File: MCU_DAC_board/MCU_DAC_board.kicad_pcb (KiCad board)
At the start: 2 copper layers, 100 x 100 mm, 95 parts, among them J1 Conn_02x04_Odd_Even, J11 105-0752-001, J12 Conn_01x03_Pin, J2 Conn_02x04_Odd_Even, J3 Conn_02x04_Odd_Even, J4 Conn_02x04_Odd_Even, J5 54-00127, J6 105-0752-001, J7 Screw_Terminal_01x02, J8 Screw_Terminal_01x02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

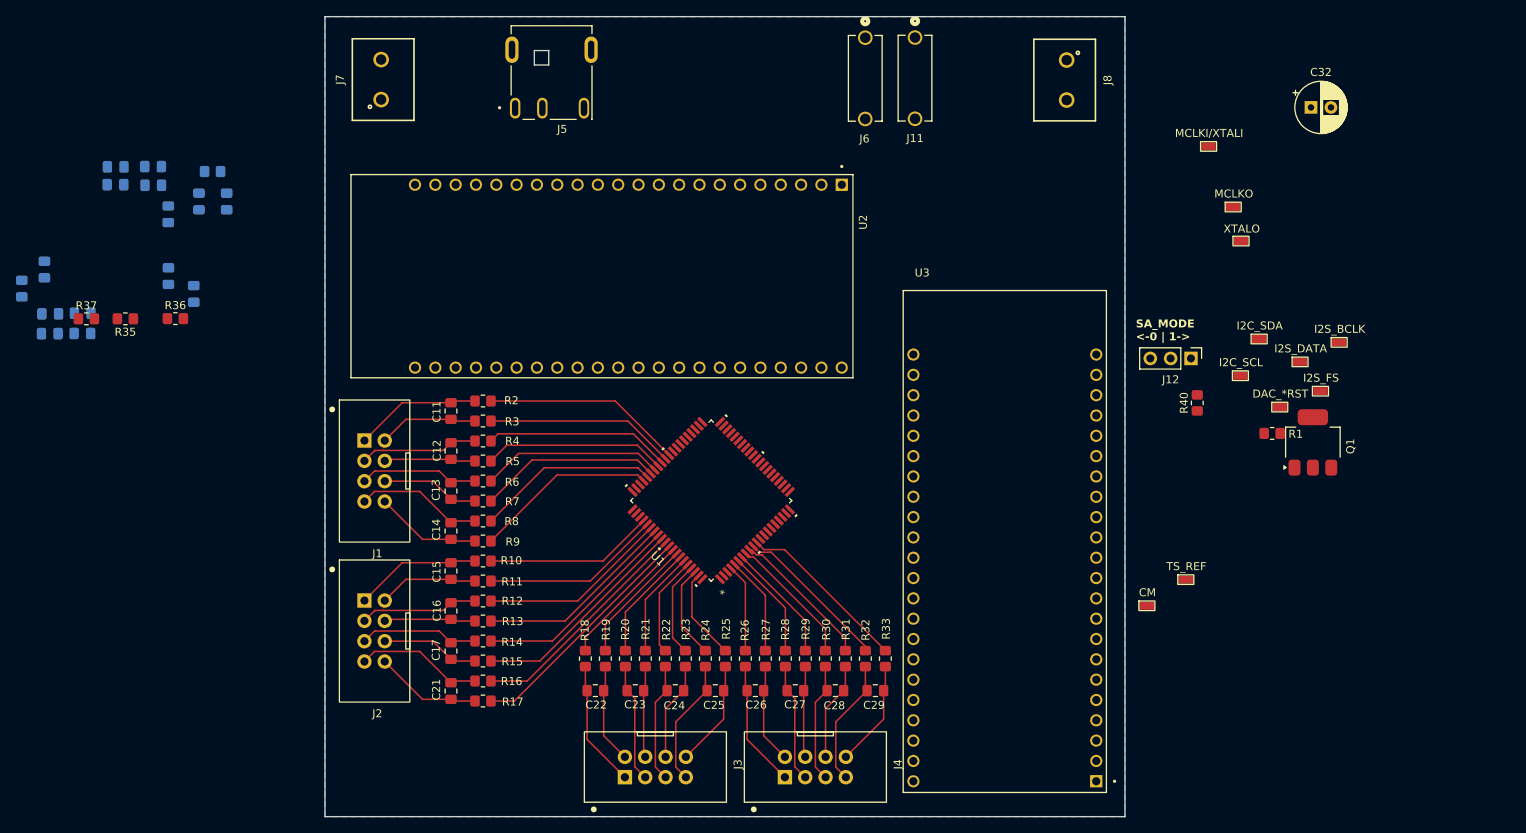
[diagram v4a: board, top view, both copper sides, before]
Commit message: Changed to 4 layer board
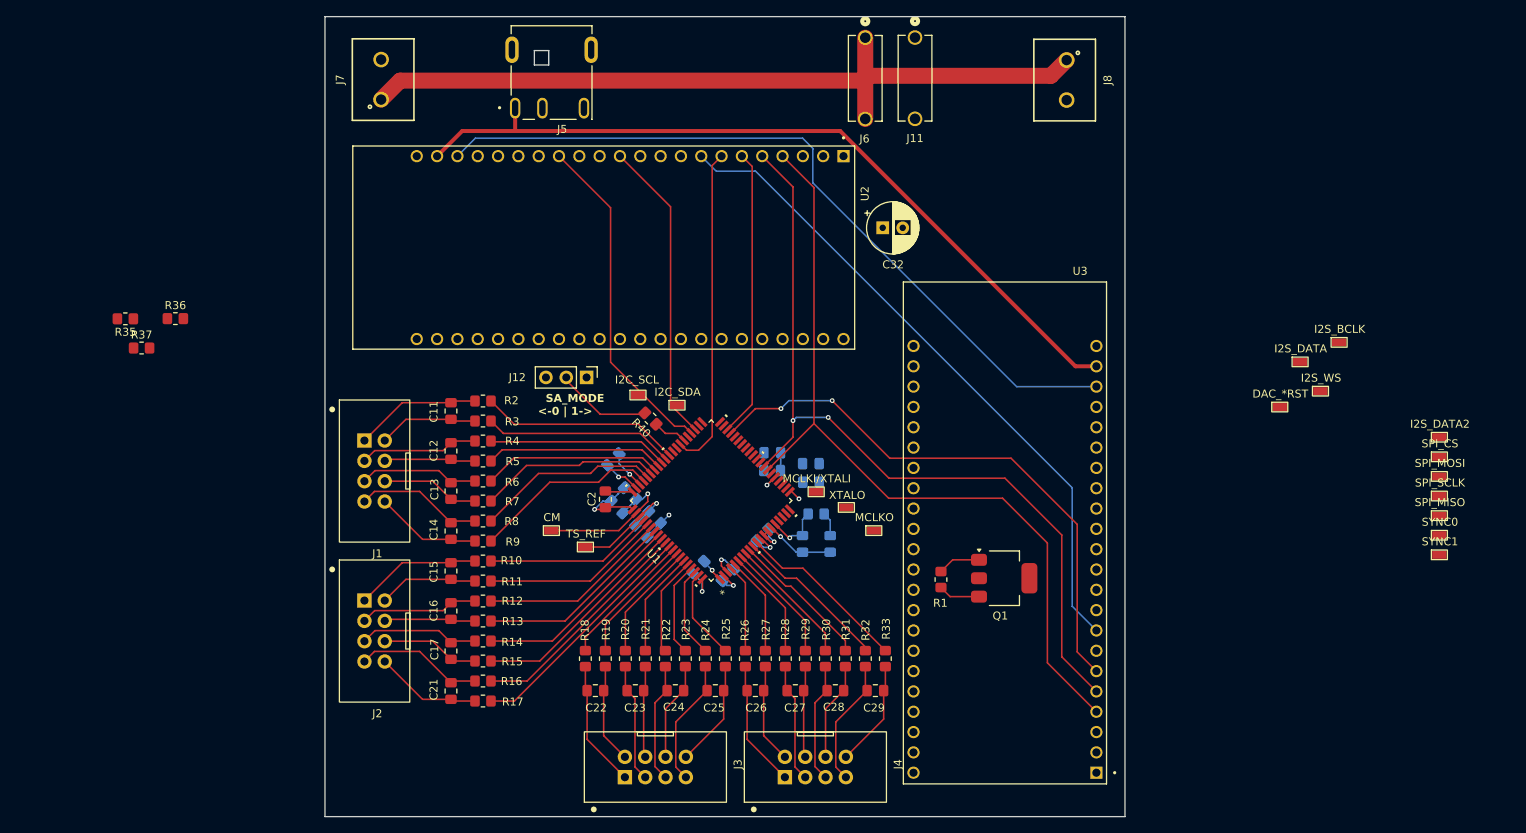
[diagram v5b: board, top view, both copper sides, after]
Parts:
- added TP12: I2S_DATA2, project_lib:TP_1.8x1mm, F.Cu at (232.4, 111.4)
- added TP13: SPI_CS, project_lib:TP_1.8x1mm, F.Cu at (232.4, 113.9)
- added TP14: SPI_MOSI, project_lib:TP_1.8x1mm, F.Cu at (232.4, 116.3)
- added TP15: SPI_SCLK, project_lib:TP_1.8x1mm, F.Cu at (232.4, 118.8)
- added TP16: SPI_MISO, project_lib:TP_1.8x1mm, F.Cu at (232.4, 121.2)
- added TP17: SYNC0, project_lib:TP_1.8x1mm, F.Cu at (232.4, 123.7)
- added TP18: SYNC1, project_lib:TP_1.8x1mm, F.Cu at (232.4, 126.1)
- C2: moved to F.Cu
- TP5: value I2S_FS -> I2S_WS
- moved C18 90.2 mm to (153.8, 114.7)
- moved C20 90.2 mm to (153.8, 117.1)
- moved C10 89.5 mm to (149.0, 115.6)
- moved C19 89.5 mm to (149.0, 113.4)
- moved C31 86.7 mm to (152.8, 124.8)
- moved C30 86.7 mm to (156.2, 124.8)
- moved R34 86.7 mm to (154.5, 121.0)
- moved C1 84.5 mm to (147.8, 123.7), turned to 45 degrees
- moved C8 79.3 mm to (143.4, 128.6), turned to 45 degrees
- moved C2 77.6 mm to (128.1, 119.2)
- moved J12 75.6 mm to (125.8, 104.0)
- moved TP9 75.3 mm to (132.2, 106.2)
- moved C5 75.3 mm to (131.2, 118.5), turned to 135 degrees
- moved TP10 75.2 mm to (125.6, 125.2)
- moved C6 75.1 mm to (134.3, 121.5), turned to -45 degrees
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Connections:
- net /GPIO6 renamed /I2S_DATA1
- Q1 pad 1: +2V5 -> /VDRIVE
- Q1 pad 2: /VDRIVE -> +2V5
- R35 pad 2: /GPIO8 -> /I2C_SDA
- R37 pad 2: /GPIO9 -> /I2C_SCL
- TP4 pad 1: /GPIO4 -> /I2S_BCLK
- TP5 pad 1: /GPIO5 -> /I2S_WS
- TP8 pad 1: /GPIO8 -> /I2C_SDA
- TP9 pad 1: /GPIO9 -> /I2C_SCL
- U1 pad 27: /GPIO4 -> /I2S_BCLK
- U1 pad 28: /GPIO5 -> /I2S_WS
- U1 pad 37: unconnected-(U1-DSDATA2-Pad37) -> /I2S_DATA2
- U1 pad 43: /GPIO8 -> /I2C_SDA
- U1 pad 44: /GPIO9 -> /I2C_SCL
- U2 pad J1_10: /GPIO17 -> unconnected-(U2-GPIO17-PadJ1_10)
- U2 pad J1_11: /GPIO18 -> unconnected-(U2-GPIO18-PadJ1_11)
- U2 pad J1_12: /GPIO8 -> /I2C_SDA
- U2 pad J1_13: /GPIO3 -> unconnected-(U2-GPIO3-PadJ1_13)
- U2 pad J1_14: /GPIO46 -> unconnected-(U2-GPIO46-PadJ1_14)
- U2 pad J1_15: /GPIO9 -> /I2C_SCL
- U2 pad J1_16: /GPIO10 -> /SPI_CS
- U2 pad J1_17: /GPIO11 -> /SPI_MOSI
- U2 pad J1_18: /GPIO12 -> /SPI_SCLK
- U2 pad J1_19: /GPIO13 -> /SPI_MISO
- U2 pad J1_20: /GPIO14 -> /SYNC0
- U2 pad J1_4: /GPIO4 -> /I2S_BCLK
- U2 pad J1_5: /GPIO5 -> /I2S_WS
- U2 pad J1_8: /GPIO15 -> /SYNC1
- U2 pad J1_9: /GPIO16 -> unconnected-(U2-GPIO16-PadJ1_9)
- U2 pad J3_10: /GPIO38 -> unconnected-(U2-GPIO38-PadJ3_10)
- U2 pad J3_11: /GPIO37 -> unconnected-(U2-GPIO37-PadJ3_11)
- U2 pad J3_12: /GPIO36 -> unconnected-(U2-GPIO36-PadJ3_12)
- U2 pad J3_13: /GPIO35 -> unconnected-(U2-GPIO35-PadJ3_13)
- U2 pad J3_14: /GPIO0 -> unconnected-(U2-GPIO0-PadJ3_14)
- U2 pad J3_15: /GPIO45 -> unconnected-(U2-GPIO45-PadJ3_15)
- U2 pad J3_16: /GPIO48 -> unconnected-(U2-GPIO48-PadJ3_16)
- U2 pad J3_17: /GPIO47 -> unconnected-(U2-GPIO47-PadJ3_17)
- U2 pad J3_18: /GPIO21 -> unconnected-(U2-GPIO21-PadJ3_18)
- U2 pad J3_19: /GPIO20 -> unconnected-(U2-USB_D+/GPIO20-PadJ3_19)
- U2 pad J3_2: /GPIO43 -> unconnected-(U2-U0TXD/GPIO43-PadJ3_2)
- U2 pad J3_20: /GPIO19 -> unconnected-(U2-USB_D-/GPIO19-PadJ3_20)
- U2 pad J3_3: /GPIO44 -> unconnected-(U2-U0RXD/GPIO44-PadJ3_3)
- U2 pad J3_4: /GPIO1 -> unconnected-(U2-GPIO1-PadJ3_4)
- U2 pad J3_5: /GPIO2 -> unconnected-(U2-GPIO2-PadJ3_5)
- U2 pad J3_6: /GPIO42 -> unconnected-(U2-MTMS/GPIO42-PadJ3_6)
- U2 pad J3_7: /GPIO41 -> unconnected-(U2-MTDI/GPIO41-PadJ3_7)
- U2 pad J3_8: /GPIO40 -> unconnected-(U2-MTDO/GPIO40-PadJ3_8)
- U2 pad J3_9: /GPIO39 -> unconnected-(U2-MTCK/GPIO39-PadJ3_9)
- U3 pad J1_12: unconnected-(U3-GPIO8-PadJ1_12) -> /I2C_SDA
- U3 pad J1_15: unconnected-(U3-GPIO9-PadJ1_15) -> /I2C_SCL
- U3 pad J1_16: unconnected-(U3-GPIO10-PadJ1_16) -> /SPI_CS
- U3 pad J1_17: unconnected-(U3-GPIO11-PadJ1_17) -> /SPI_MOSI
- U3 pad J1_18: unconnected-(U3-GPIO12-PadJ1_18) -> /SPI_SCLK
- U3 pad J1_19: unconnected-(U3-GPIO13-PadJ1_19) -> /SPI_MISO
- U3 pad J1_20: unconnected-(U3-GPIO14-PadJ1_20) -> /SYNC0
- U3 pad J1_21: unconnected-(U3-5V0-PadJ1_21) -> +5V
- U3 pad J1_22: unconnected-(U3-GND-PadJ1_22) -> GND
- U3 pad J1_4: unconnected-(U3-GPIO4-PadJ1_4) -> /I2S_BCLK
- U3 pad J1_5: unconnected-(U3-GPIO5-PadJ1_5) -> /I2S_WS
- U3 pad J1_6: unconnected-(U3-GPIO6-PadJ1_6) -> /I2S_DATA2
- U3 pad J1_7: unconnected-(U3-GPIO7-PadJ1_7) -> /DAC_*RST
- U3 pad J1_8: unconnected-(U3-GPIO15-PadJ1_8) -> /SYNC1
- U3 pad J3_1: unconnected-(U3-GND__1-PadJ3_1) -> GND
- U3 pad J3_21: unconnected-(U3-GND__2-PadJ3_21) -> GND
- U3 pad J3_22: unconnected-(U3-GND__3-PadJ3_22) -> GND
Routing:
- net /I2S_WS: track 0.00 -> 103.0 mm, vias 0 -> 2
- net /I2S_BCLK: track 0.00 -> 102.2 mm
- net +5V: track 0.00 -> 98.8 mm
- net +24V: track 0.00 -> 97.9 mm
- net /SYNC0: track 0.00 -> 96.2 mm
- net /SYNC1: track 0.00 -> 82.6 mm
- net /I2S_DATA2: track 0.00 -> 70.7 mm, vias 0 -> 2
- net /I2C_SCL: track 0.00 -> 42.2 mm
- net /DAC_*RST: track 0.00 -> 40.5 mm
- net /I2C_SDA: track 0.00 -> 38.0 mm
- net /I2S_DATA1: track 0.00 -> 36.0 mm
- net +3V3: track 0.00 -> 23.8 mm, vias 0 -> 4
- net GND: track 0.00 -> 23.5 mm, vias 0 -> 5
- net Net-(U1-CM): track 0.00 -> 18.6 mm, vias 0 -> 1
- net Net-(U1-TS_REF): track 0.00 -> 15.0 mm, vias 0 -> 1
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- added copper zone on In2.Cu, net +3V3
- added copper zone on In1.Cu, net GND
- removed copper zone on B.Cu, net GND
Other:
- copper layers 2 -> 4

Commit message: Amp board final draft
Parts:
- moved R35 80.5 mm to (148.6, 93.1), turned to 90 degrees
- moved R36 78.2 mm to (152.5, 94.9), turned to -90 degrees
- moved R37 74.2 mm to (143.8, 91.5)
- moved J7 32.2 mm to (132.3, 66.5), turned to -90 degrees
- moved J5 20.7 mm to (100.7, 63.7)
- moved Q1 11.7 mm to (178.3, 117.4)
- moved R1 11.7 mm to (170.4, 117.6)
- moved TP12 11.5 mm to (236.6, 100.7)
- moved TP13 11.5 mm to (236.6, 103.2)
- moved TP17 11.5 mm to (236.6, 113.0)
- moved TP18 11.5 mm to (236.6, 115.4)
- moved TP4 11.5 mm to (224.0, 88.8)
- moved TP6 11.5 mm to (216.6, 96.9)
- moved TP14 11.5 mm to (236.6, 105.6)
- moved TP15 11.5 mm to (236.6, 108.1)
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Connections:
- U2 pad J1_12: /I2C_SDA -> unconnected-(U2-GPIO8-PadJ1_12)
- U2 pad J1_15: /I2C_SCL -> unconnected-(U2-GPIO9-PadJ1_15)
- U2 pad J1_16: /SPI_CS -> unconnected-(U2-GPIO10-PadJ1_16)
- U2 pad J1_17: /SPI_MOSI -> unconnected-(U2-GPIO11-PadJ1_17)
- U2 pad J1_18: /SPI_SCLK -> unconnected-(U2-GPIO12-PadJ1_18)
- U2 pad J1_19: /SPI_MISO -> unconnected-(U2-GPIO13-PadJ1_19)
- U2 pad J1_20: /SYNC0 -> unconnected-(U2-GPIO14-PadJ1_20)
- U2 pad J1_4: /I2S_BCLK -> unconnected-(U2-GPIO4-PadJ1_4)
- U2 pad J1_5: /I2S_WS -> unconnected-(U2-GPIO5-PadJ1_5)
- U2 pad J1_6: /I2S_DATA1 -> unconnected-(U2-GPIO6-PadJ1_6)
- U2 pad J1_7: /DAC_*RST -> unconnected-(U2-GPIO7-PadJ1_7)
- U2 pad J1_8: /SYNC1 -> unconnected-(U2-GPIO15-PadJ1_8)
- U2 pad J3_2: unconnected-(U2-U0TXD/GPIO43-PadJ3_2) -> /USART_TX
- U2 pad J3_3: unconnected-(U2-U0RXD/GPIO44-PadJ3_3) -> /USART_RX
- U2 pad J3_4: unconnected-(U2-GPIO1-PadJ3_4) -> /I2S_BCLK
- U2 pad J3_5: unconnected-(U2-GPIO2-PadJ3_5) -> /I2S_WS
- U2 pad J3_6: unconnected-(U2-MTMS/GPIO42-PadJ3_6) -> /I2S_DATA1
- U2 pad J3_7: unconnected-(U2-MTDI/GPIO41-PadJ3_7) -> /DAC_*RST
- U2 pad J3_8: unconnected-(U2-MTDO/GPIO40-PadJ3_8) -> /I2C_SDA
- U2 pad J3_9: unconnected-(U2-MTCK/GPIO39-PadJ3_9) -> /I2C_SCL
- U3 pad J1_12: /I2C_SDA -> unconnected-(U3-GPIO8-PadJ1_12)
- U3 pad J1_15: /I2C_SCL -> unconnected-(U3-GPIO9-PadJ1_15)
- U3 pad J1_16: /SPI_CS -> unconnected-(U3-GPIO10-PadJ1_16)
- U3 pad J1_17: /SPI_MOSI -> unconnected-(U3-GPIO11-PadJ1_17)
- U3 pad J1_18: /SPI_SCLK -> unconnected-(U3-GPIO12-PadJ1_18)
- U3 pad J1_19: /SPI_MISO -> unconnected-(U3-GPIO13-PadJ1_19)
- U3 pad J1_20: /SYNC0 -> unconnected-(U3-GPIO14-PadJ1_20)
- U3 pad J1_4: /I2S_BCLK -> /I2C_SCL
- U3 pad J1_5: /I2S_WS -> /I2C_SDA
- U3 pad J1_6: /I2S_DATA2 -> /DAC_*RST
- U3 pad J1_7: /DAC_*RST -> /I2S_DATA2
- U3 pad J1_8: /SYNC1 -> unconnected-(U3-GPIO15-PadJ1_8)
- U3 pad J3_2: unconnected-(U3-U0TXD/GPIO43-PadJ3_2) -> /USART_RX
- U3 pad J3_3: unconnected-(U3-U0RXD/GPIO44-PadJ3_3) -> /USART_TX
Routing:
- net +5V: track 98.8 -> 0.00 mm
- net /SYNC0: track 96.2 -> 0.00 mm
- net /I2S_WS: track 103.0 -> 18.0 mm, vias 2 -> 0
- net /I2S_BCLK: track 102.2 -> 18.4 mm
- net /SYNC1: track 82.6 -> 0.00 mm
- net /I2S_DATA2: track 70.7 -> 23.7 mm, vias 2 -> 1
- net /USART_RX: track 0.00 -> 43.0 mm
- net /USART_TX: track 0.00 -> 40.4 mm
- net +2V5: track 7.24 -> 36.4 mm, vias 1 -> 3
- net /I2S_DATA1: track 36.0 -> 12.0 mm
- net GND: track 23.5 -> 39.9 mm, vias 5 -> 9
- net +3V3: track 23.8 -> 38.9 mm, vias 4 -> 10
- net /MCLKO: track 0.00 -> 11.4 mm
- net /I2C_SDA: track 38.0 -> 46.3 mm
- net /XTALO: track 0.00 -> 7.69 mm
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
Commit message: Widened 24V trace, added triple vias for 3V3 lines, and other things
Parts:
- moved R36 1.45 mm to (154.0, 94.9)
- moved R35 0.90 mm to (147.7, 93.1)
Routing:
- net +3V3: track 38.9 -> 218.2 mm, vias 10 -> 20
- net +5V: track 0.00 -> 162.6 mm
- net +24V: track 97.9 -> 65.4 mm
- net +2V5: track 36.4 -> 68.4 mm, vias 3 -> 5
- net /VDRIVE: track 0.00 -> 5.36 mm
- net /DAC_*RST: track 47.1 -> 45.9 mm, vias 0 -> 1
- net /I2S_DATA2: track 23.7 -> 24.9 mm
- net Net-(U1-DAC_BIAS1): track 4.82 -> 5.67 mm

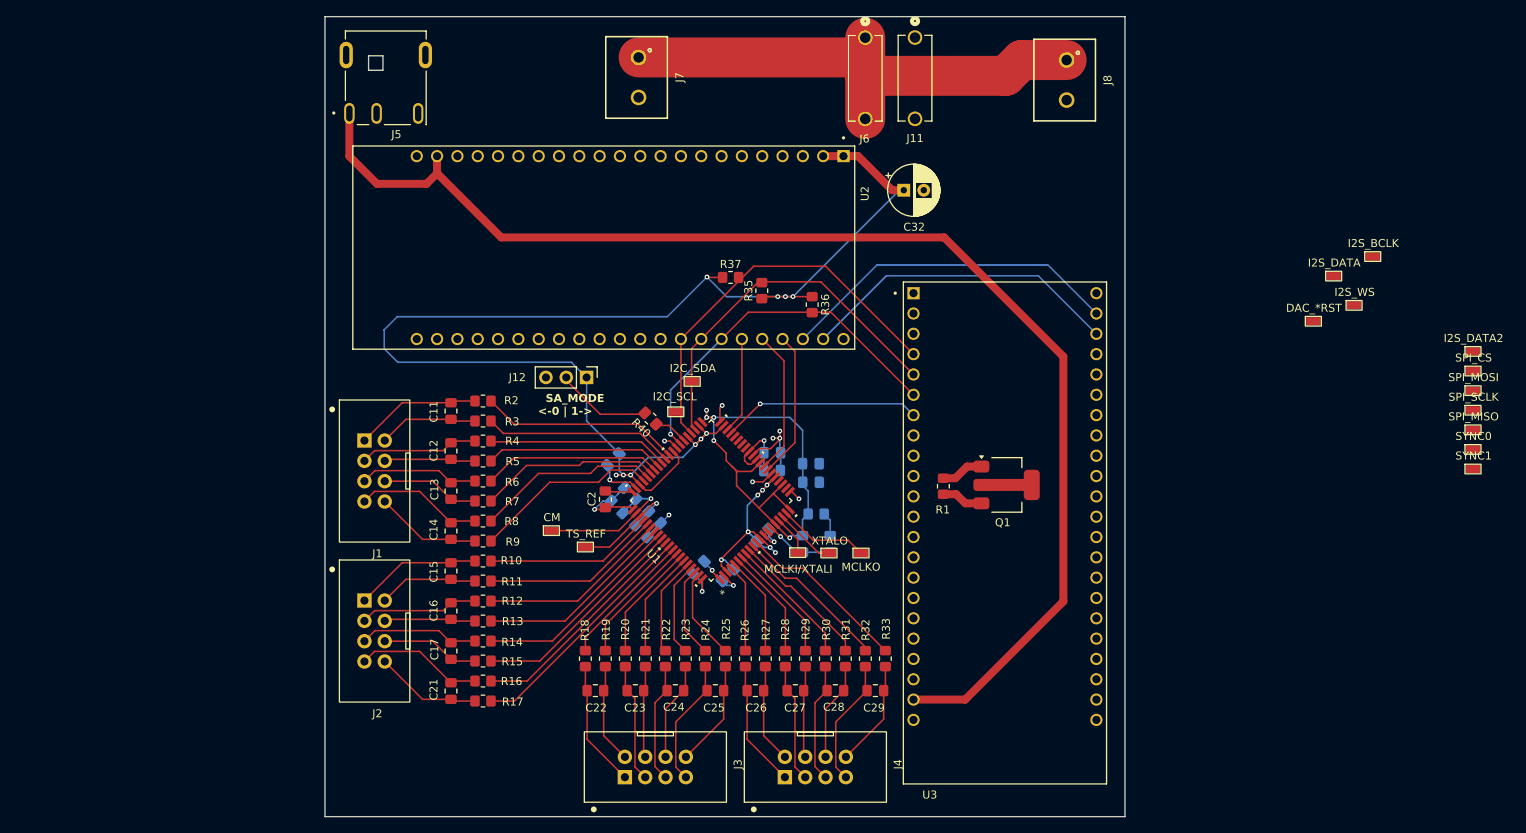
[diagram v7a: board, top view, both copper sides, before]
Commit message: made power lines heavier and added most of the test points
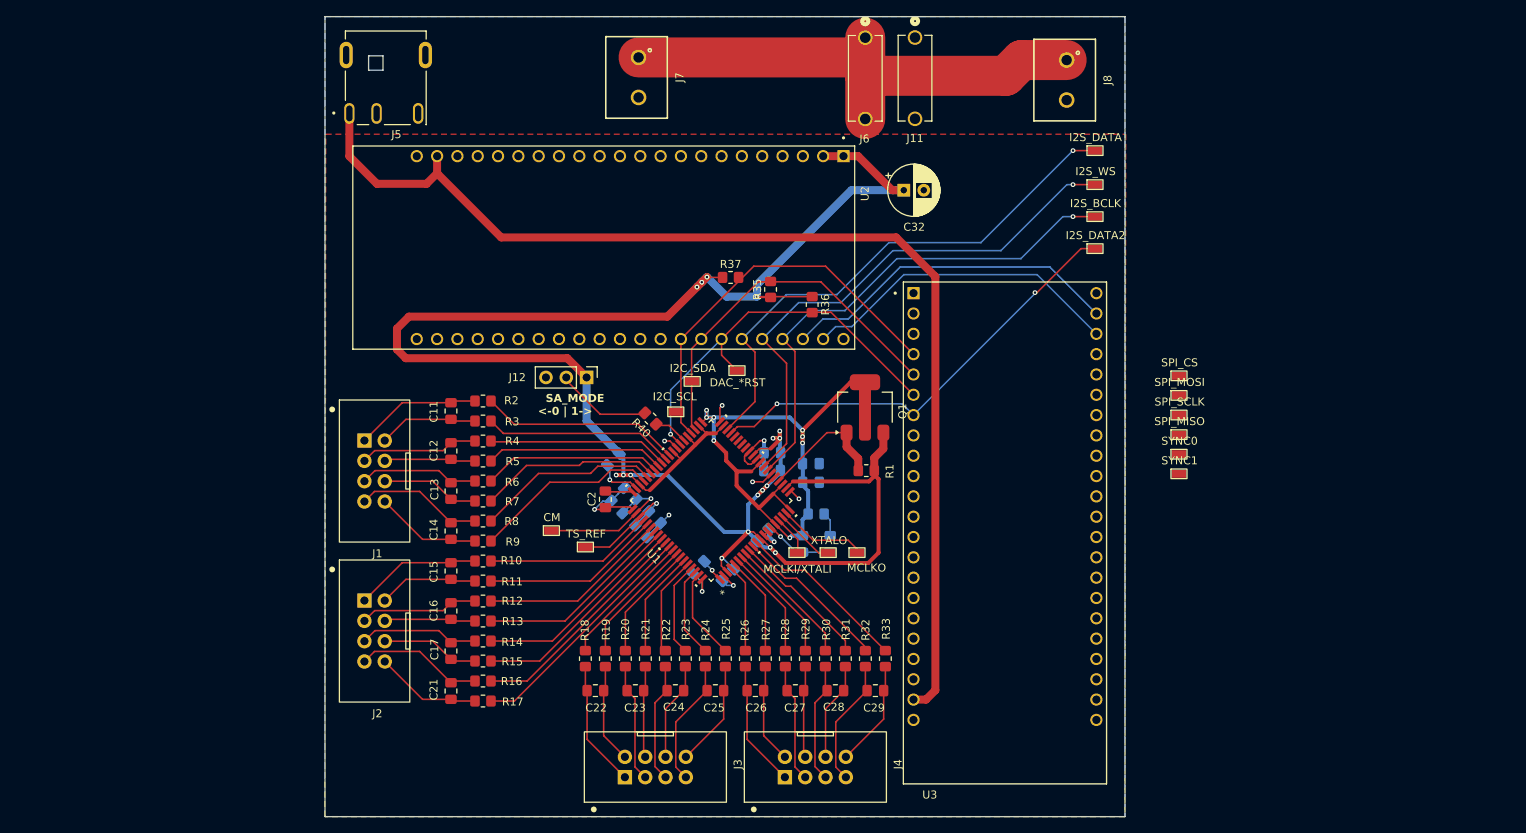
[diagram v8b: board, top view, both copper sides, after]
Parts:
- moved TP6 72.3 mm to (144.6, 103.1)
- moved TP12 49.0 mm to (189.3, 87.9)
- moved TP13 36.8 mm to (199.8, 103.8)
- moved TP14 36.8 mm to (199.8, 106.2)
- moved TP15 36.8 mm to (199.8, 108.7)
- moved TP16 36.8 mm to (199.8, 111.1)
- moved TP17 36.8 mm to (199.8, 113.6)
- moved TP18 36.8 mm to (199.8, 116.0)
- moved TP5 35.7 mm to (189.3, 79.9)
- moved TP4 35.1 mm to (189.3, 83.9)
- moved TP7 33.7 mm to (189.3, 75.6)
- moved Q1 20.2 mm to (160.6, 107.7), turned to 90 degrees
- moved R1 9.83 mm to (160.7, 115.6), turned to 180 degrees
- moved R35 1.11 mm to (148.8, 93.0)
- moved TP3 0.50 mm to (159.6, 125.9)
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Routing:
- net /I2S_DATA1: track 12.0 -> 67.3 mm, vias 0 -> 1
- net /I2S_WS: track 18.0 -> 67.9 mm, vias 0 -> 1
- net +3V3: track 218.2 -> 266.0 mm, vias 20 -> 17
- net /I2S_BCLK: track 18.4 -> 63.8 mm, vias 0 -> 1
- net /I2S_DATA2: track 24.9 -> 56.3 mm, vias 1 -> 2
- net +5V: track 162.6 -> 143.0 mm
- net +2V5: track 68.4 -> 79.4 mm, vias 5 -> 8
- net /VDRIVE: track 5.36 -> 16.3 mm
- net /DAC_*RST: track 45.9 -> 50.7 mm
- added copper zone on B.Cu, net GND
- added copper zone on F.Cu, net GND
- added copper zone on In2.Cu, net GND
- removed copper zone on In2.Cu, net +3V3
